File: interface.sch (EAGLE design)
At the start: 9 parts, among them U1 LCD-16X2

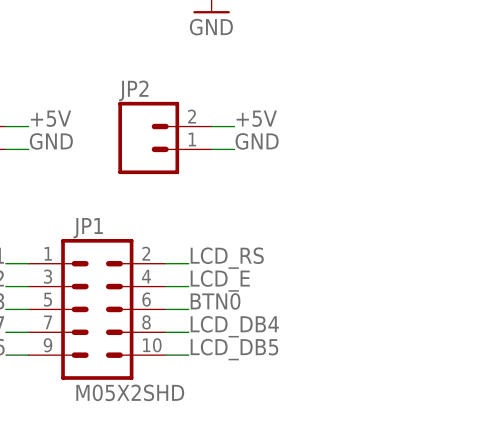
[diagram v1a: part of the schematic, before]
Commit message: Added header for spare pin from 10pin connector.
Added a 2pin header to allow access to the "spare" pin on the 10 pin
header.
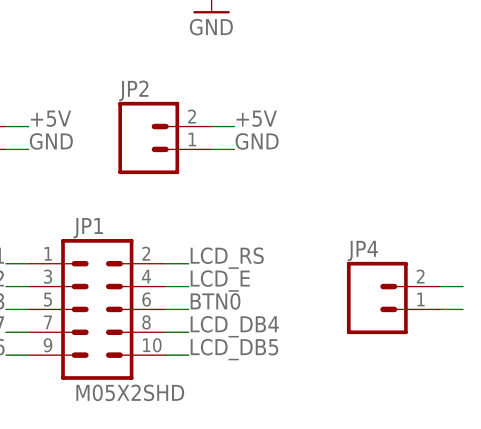
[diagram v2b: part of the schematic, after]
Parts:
- added JP4: (no value), SparkFun-Connectors:M02PTH
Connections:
- net BTN3: now also JP4.2
- net GND: now also JP4.1
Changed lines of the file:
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@@
 <part name="GND4" library="supply1" deviceset="GND" device=""/>
 <part name="JP3" library="SparkFun-Connectors" deviceset="M02" device="PTH"/>
+<part name="JP4" library="SparkFun-Connectors" deviceset="M02" device="PTH"/>
 </parts>
 <sheets>
@@
 <instance part="GND4" gate="1" x="127" y="43.18"/>
 <instance part="JP3" gate="G$1" x="96.52" y="27.94"/>
+<instance part="JP4" gate="G$1" x="144.78" y="10.16"/>
 </instances>
 <busses>
@@
 <label x="104.14" y="10.16" size="1.778" layer="95" rot="MR0"/>
 </segment>
+<segment>
+<pinref part="JP4" gate="G$1" pin="2"/>
+<wire x1="152.4" y1="12.7" x2="154.94" y2="12.7" width="0.1524" layer="91"/>
+</segment>
 </net>
 <net name="LCD_DB7" class="0">
@@
 <label x="106.68" y="27.94" size="1.778" layer="95"/>
 </segment>
-</net>
+<segment>
+<pinref part="JP4" gate="G$1" pin="1"/>
+<wire x1="152.4" y1="10.16" x2="154.94" y2="10.16" width="0.1524" layer="91"/>
+</segment>
+</net>

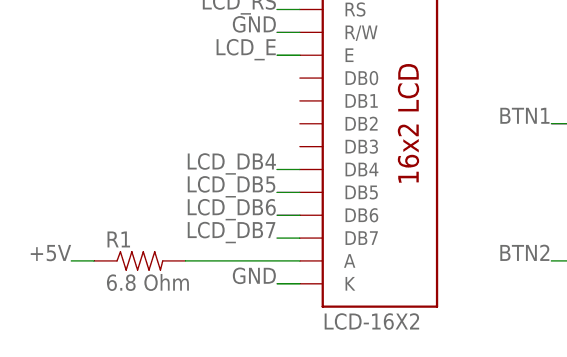
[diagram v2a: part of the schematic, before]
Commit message: Changed 1 of the aux power connectors to molex polarized header.
Made change for interface and for controller boards
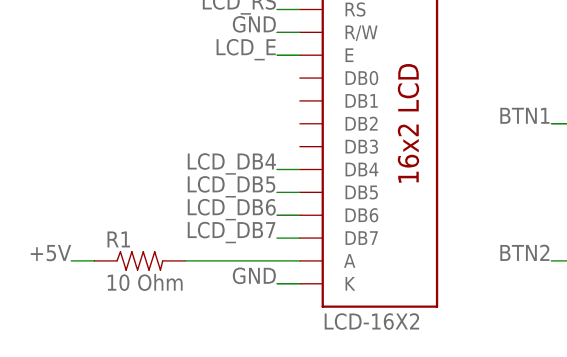
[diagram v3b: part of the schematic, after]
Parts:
- JP2: device SparkFun-Connectors:M02PTH -> SparkFun-Connectors:M02POLAR
- R1: value 6.8 Ohm -> 10 Ohm
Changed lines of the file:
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@@
 <part name="GND2" library="supply1" deviceset="GND" device=""/>
 <part name="GND3" library="supply1" deviceset="GND" device=""/>
-<part name="JP2" library="SparkFun-Connectors" deviceset="M02" device="PTH"/>
-<part name="R1" library="SparkFun-Resistors" deviceset="RESISTOR" device="1206" value="6.8 Ohm"/>
+<part name="JP2" library="SparkFun-Connectors" deviceset="M02" device="POLAR"/>
+<part name="R1" library="SparkFun-Resistors" deviceset="RESISTOR" device="1206" value="10 Ohm"/>
 <part name="R2" library="SparkFun-Electromechanical" deviceset="TRIMPOT" device="-2" value="TRIMPOT-10k"/>
 <part name="GND4" library="supply1" deviceset="GND" device=""/>

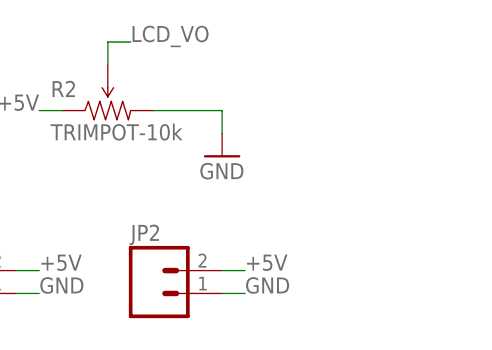
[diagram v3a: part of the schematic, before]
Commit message: Updated some layout, added logo
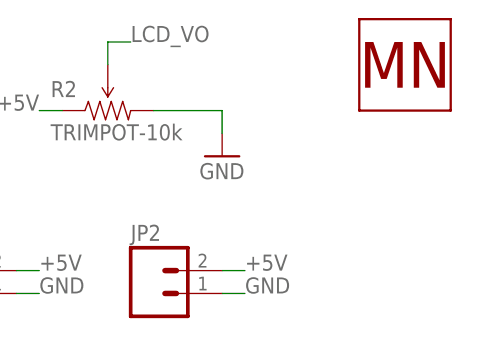
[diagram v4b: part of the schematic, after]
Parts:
- added U$5: MN-LOGO, Mikes-Aesthetics:MN-LOGO
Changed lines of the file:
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@@
 <part name="JP3" library="SparkFun-Connectors" deviceset="M02" device="PTH"/>
 <part name="JP4" library="SparkFun-Connectors" deviceset="M02" device="PTH"/>
+<part name="U$5" library="Mikes-Aesthetics" deviceset="MN-LOGO" device=""/>
 </parts>
 <sheets>
@@
 <instance part="JP3" gate="G$1" x="96.52" y="27.94"/>
 <instance part="JP4" gate="G$1" x="144.78" y="10.16"/>
+<instance part="U$5" gate="G$1" x="147.32" y="53.34"/>
 </instances>
 <busses>
